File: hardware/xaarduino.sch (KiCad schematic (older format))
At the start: 3 parts

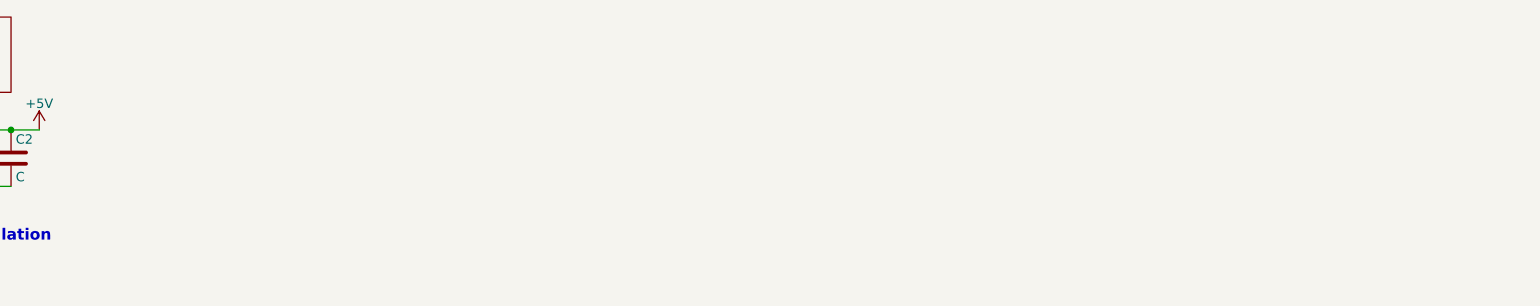
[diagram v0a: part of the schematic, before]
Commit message: first pass at xaar header
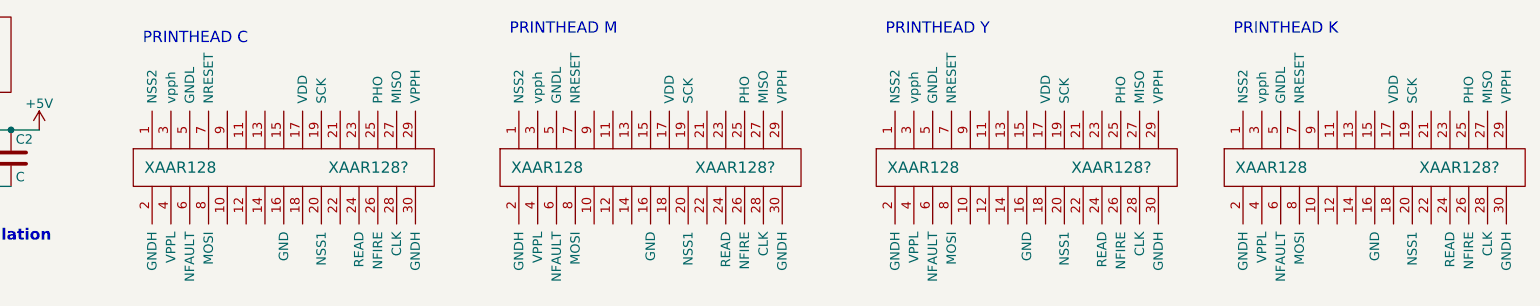
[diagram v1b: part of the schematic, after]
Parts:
- added XAAR128? (x4): XAAR128, symbol XAAR128
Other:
- note added: "PRINTHEAD C"
- note added: "PRINTHEAD K"
- note added: "PRINTHEAD M"
- note added: "PRINTHEAD Y"
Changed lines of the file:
@@
 LIBS:valves
 LIBS:xaarduino
+LIBS:xaarduino-cache
 EELAYER 25 0
 EELAYER END
@@
 Text Notes 650  1750 0    60   ~ 12
 TTL Power Regulation
+$Comp
+L XAAR128 XAAR128?
+U 1 1 5A3D5B8D
+P 2850 1350
+F 0 "XAAR128?" H 3350 1350 60  0000 C CNN
+F 1 "XAAR128" H 2350 1350 60  0000 C CNN
+F 2 "" H 3500 850 60  0001 C CNN
+F 3 "" H 3500 850 60  0001 C CNN
+	1    2850 1350
+	1    0    0    -1
+$EndComp
+Text Notes 2150 700  0    60   ~ 0
+PRINTHEAD C
+$Comp
+L XAAR128 XAAR128?
+U 1 1 5A3D5BCF
+P 4800 1350
+F 0 "XAAR128?" H 5300 1350 60  0000 C CNN
+F 1 "XAAR128" H 4300 1350 60  0000 C CNN
+F 2 "" H 5450 850 60  0001 C CNN
+F 3 "" H 5450 850 60  0001 C CNN
+	1    4800 1350
+	1    0    0    -1
+$EndComp
+$Comp
+L XAAR128 XAAR128?
+U 1 1 5A3D5BFA
+P 6800 1350
+F 0 "XAAR128?" H 7300 1350 60  0000 C CNN
+F 1 "XAAR128" H 6300 1350 60  0000 C CNN
+F 2 "" H 7450 850 60  0001 C CNN
+F 3 "" H 7450 850 60  0001 C CNN
+	1    6800 1350
+	1    0    0    -1
+$EndComp
+Text Notes 4100 650  0    60   ~ 0
+PRINTHEAD M
+Text Notes 6100 650  0    60   ~ 0
+PRINTHEAD Y
+$Comp
+L XAAR128 XAAR128?
+U 1 1 5A3D5C75
+P 8650 1350
+F 0 "XAAR128?" H 9150 1350 60  0000 C CNN
+F 1 "XAAR128" H 8150 1350 60  0000 C CNN
+F 2 "" H 9300 850 60  0001 C CNN
+F 3 "" H 9300 850 60  0001 C CNN
+	1    8650 1350
+	1    0    0    -1
+$EndComp
+Text Notes 7950 650  0    60   ~ 0
+PRINTHEAD K
 $EndSCHEMATC

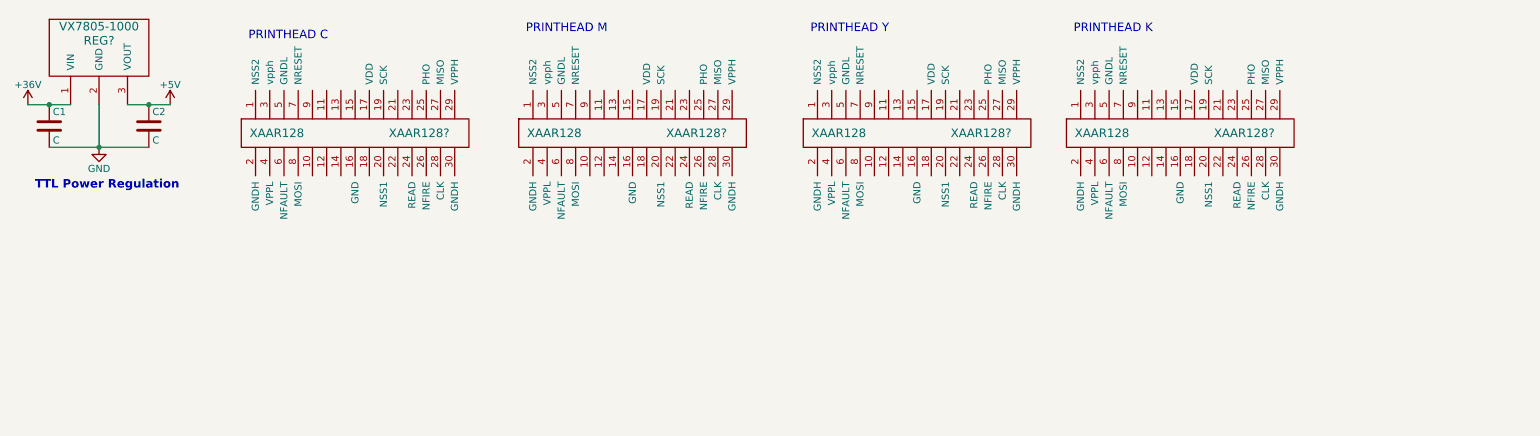
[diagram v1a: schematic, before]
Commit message: working up 35v control circuit
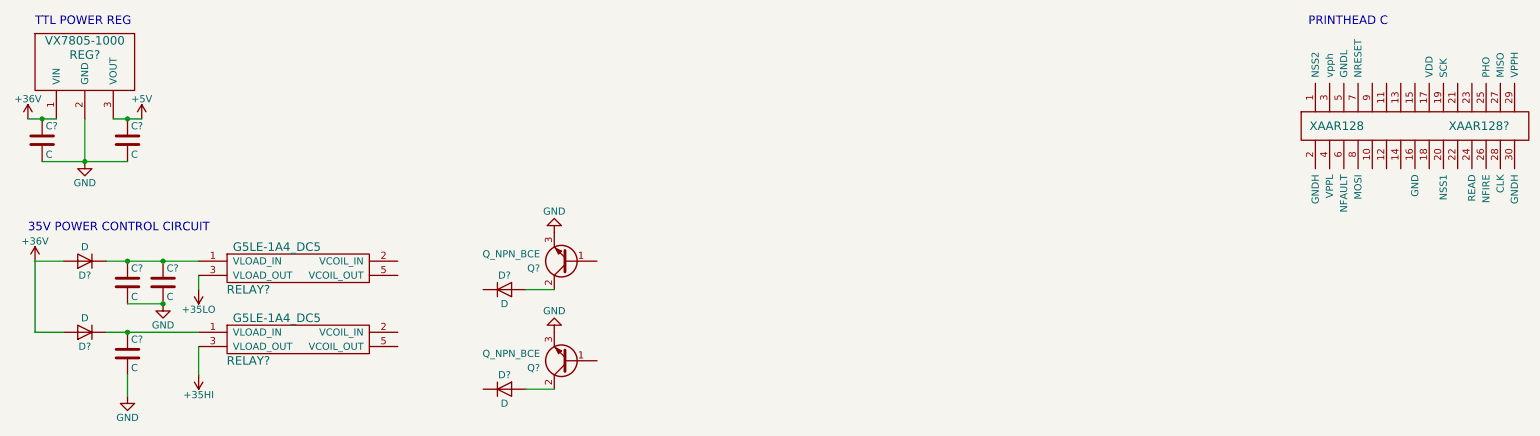
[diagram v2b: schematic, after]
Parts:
- removed C1, C2: C, symbol C
- removed REG?: VX7805-1000, symbol VX7805-1000
- removed XAAR128? (x3): XAAR128, symbol XAAR128
- added C? (x5): C, symbol C
- added D? (x4): D, symbol D
- added Q? (x2): Q_NPN_BCE, symbol Q_NPN_BCE
- added REG?: VX7805-1000, symbol VX7805-1000
- added RELAY? (x2): G5LE-1A4_DC5, symbol G5LE-1A4_DC5
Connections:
- net +36V: now also C?.1, D?.2 (A), D?.2 (A), REG?.1 (VIN)
- net +5V: now also C?.1, REG?.3 (VOUT)
- net GND: now also C?.2, C?.2, C?.2, C?.2, C?.2, Q?.3 (E), Q?.3 (E), REG?.2 (GND)
- new net: C?.1, C?.1, D?.1 (K), RELAY?.1 (VLOAD_IN)
- new net: C?.1, D?.1 (K), RELAY?.1 (VLOAD_IN)
- new net: D?.2 (A), Q?.2 (C) (x2)
- new net +35H: RELAY?.3 (VLOAD_OUT)
- new net +35LO: RELAY?.3 (VLOAD_OUT)
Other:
- note added: "35V POWER CONTROL CIRCUIT"
- note added: "TTL POWER REG"
- note removed: "PRINTHEAD K"
- note removed: "PRINTHEAD M"
- note removed: "PRINTHEAD Y"
- note removed: "TTL Power Regulation"
- moved on the sheet: XAAR128?
